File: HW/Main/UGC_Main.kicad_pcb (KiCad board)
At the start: 4 copper layers, 125.7 x 76.4 mm, 135 parts, among them J1 Rumble, J10 Conn_01x01_Pin, J11 Conn_01x01_Pin, J12 Conn_01x01_Pin, J13 503480-0640, J14 USB4105-GF-A-060, J2 LT, J3 RT, J4 Conn_01x06_Pin, J5 Conn_01x01_Pin, J6 Conn_01x01_Pin, J7 Conn_01x01_Pin, J8 Conn_01x01_Pin, J9 Conn_01x01_Pin, Q1 MMBT3904, Q2 MMBT3904, Q3 BSS138DW, Q4 BSS138DW, Q5 Q_NMOS_GSD, Q6 Q_PMOS_GDS, Q7 Q_NMOS_GSD, SW1 SW_Push, SW10 SW_Push, SW11 SW_Push, SW12 SW_Push, SW13 SW_Push, SW14 TS09-63-25-R-260-SMT, SW2 SW_Push, SW3 SW_Push, SW4 SW_Push, SW5 SW_Push, SW6 GL18_SW, SW7 SW_Push, SW8 SW_Push, SW9 TS09-63-25-R-260-SMT, U1 ESP32-PICO-MINI-02, U10 ST_LSM6, U11 BQ25180, U12 CH340K, U13 PI3USB4000A, U2 GH39F (Hall SOT23), U3 GH39F (Hall SOT23), U4 TPS630001RCR, U5 ST_LSM6, U6 MCP3002, U7 MCP3002, U8 RP2040, U9 GD25Q80EEIGR, Y1 Crystal_GND3

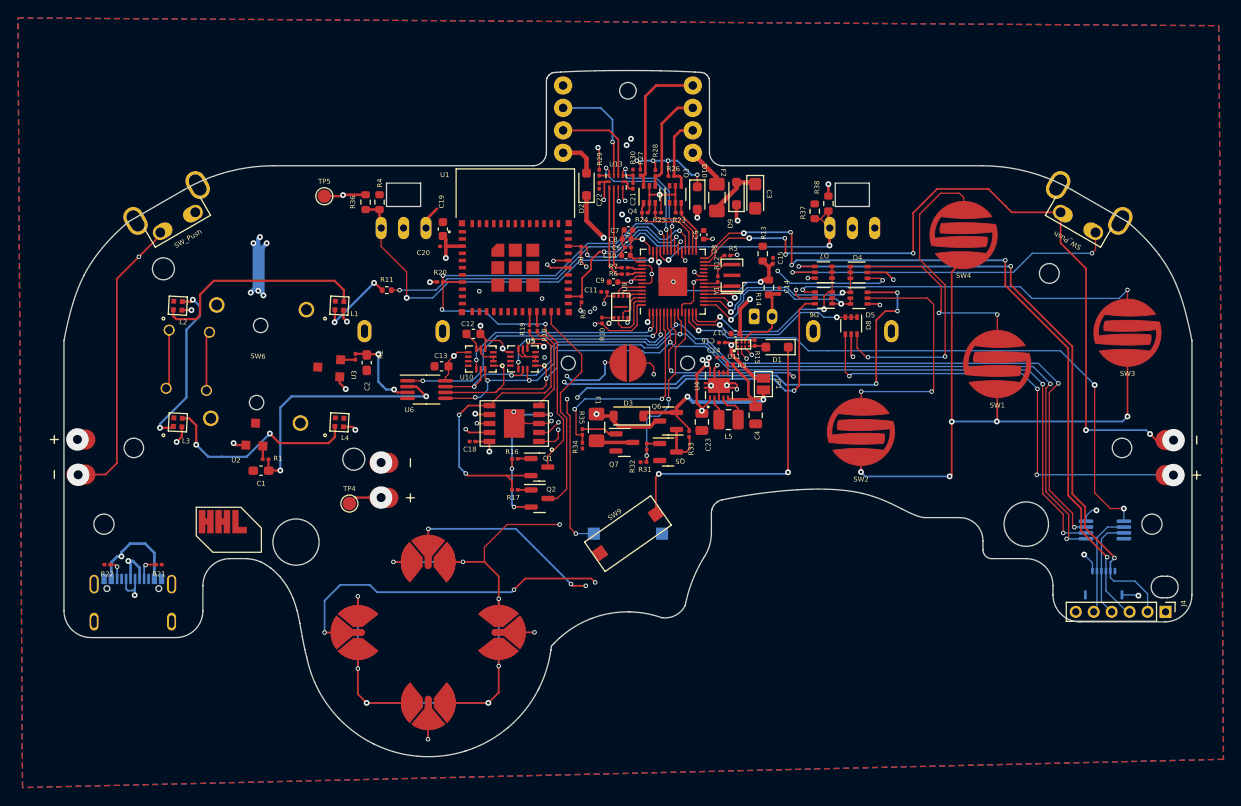
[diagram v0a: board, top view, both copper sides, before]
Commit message: Unify USB C connector
Unified USB-C Connection
Reliability issues present with type C pogo pin board
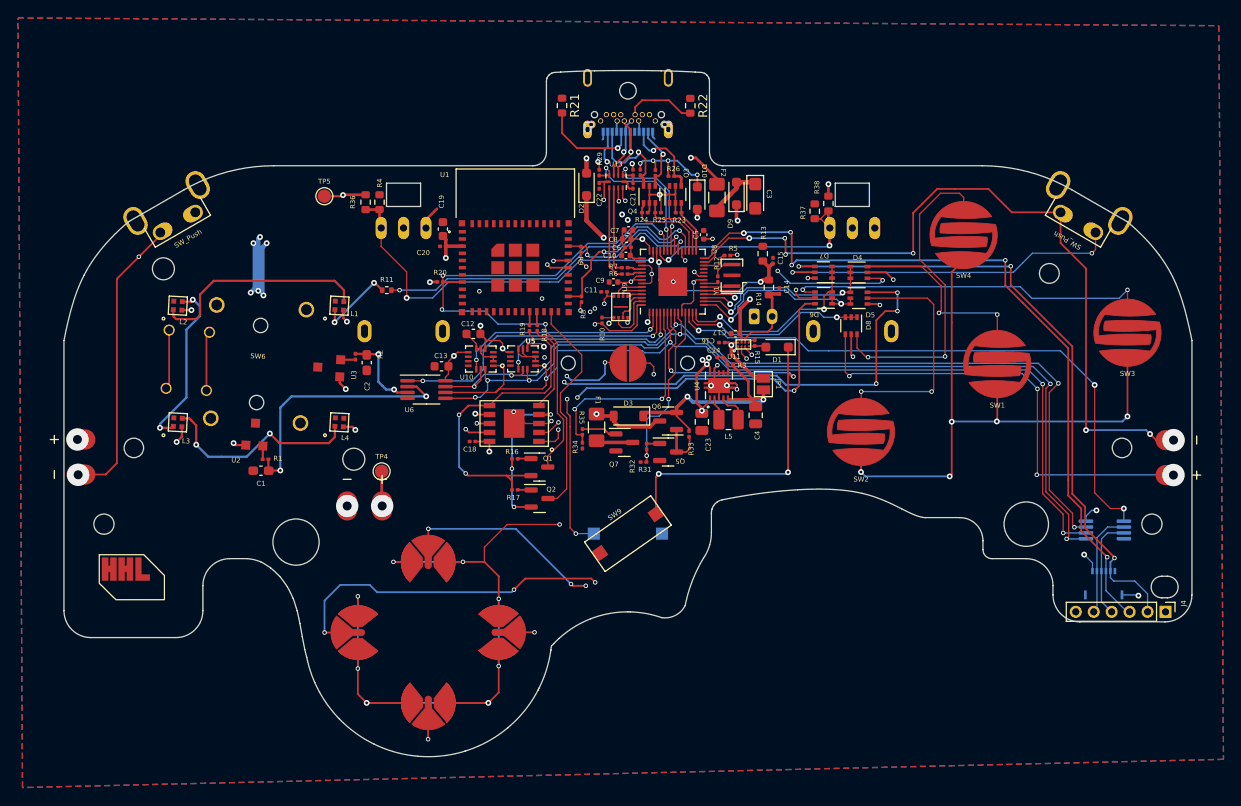
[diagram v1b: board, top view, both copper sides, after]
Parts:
- removed J10, J11, J12, J6, J7, J8, J9: Conn_01x01_Pin, hhl:YZ72015053P-01
- removed J14: USB4105-GF-A-060, hhl:GCT_USB4105-GF-A-060
- J5: value Conn_01x01_Pin -> UJ31-CH-G1-SMT-TR; footprint hhl:YZ72015053P-01 -> hhl:CUI_UJ31-CH-G1-SMT-TR
- R21, R22: value 5.1k -> 5.1kohm; footprint Resistor_SMD:R_0201_0603Metric -> Resistor_SMD:R_0603_1608Metric
- moved R22 82.7 mm to (225.4, 87.8), turned to -90 degrees
- moved R21 68.1 mm to (211.1, 87.8), turned to -90 degrees
- moved REF** 12.0 mm to (162.5, 140.8)
- moved J5 6.83 mm to (215.7, 90.7), turned to 0 degrees
- moved TP4 5.07 mm to (191.0, 128.6)
- moved J1 1.96 mm to (190.3, 132.4), turned to -90 degrees
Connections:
- R21 pad 2: Net-(J14-CC1) -> CC1
- R22 pad 1: Net-(J14-CC2) -> GND
- R22 pad 2: GND -> CC2
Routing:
- net D+: track 120.5 -> 6.93 mm, vias 2 -> 1
- net D-: track 113.1 -> 9.27 mm
- net +5V_PRE: track 110.0 -> 14.8 mm
- net +3V3_PRE: track 4.62 -> 23.1 mm, vias 0 -> 2
- net CC1: track 0.00 -> 11.1 mm, vias 0 -> 1
- net N_LATCH: track 8.51 -> 16.7 mm, vias 0 -> 1
- net CC2: track 0.00 -> 7.89 mm
- net RUMBLE-: track 35.5 -> 42.5 mm
- net N_DATA: track 11.6 -> 16.2 mm, vias 0 -> 1
- net Net-(J14-CC1): track 2.79 -> 0.00 mm, vias 1 -> 0
- net Net-(J14-CC2): track 2.23 -> 0.00 mm, vias 1 -> 0
- net VBUS_SYS: track 102.2 -> 103.4 mm
- net GND: track 40.4 -> 41.3 mm, vias 19 -> 18
- net SHARED_PU: track 12.8 -> 12.1 mm
- net N_CLOCK: track 16.2 -> 16.0 mm, vias 0 -> 1

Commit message: PCB Update
- Add RESET switch
- Add ESP bootloader switch
- Adjust screw holes for trigger bracket mount
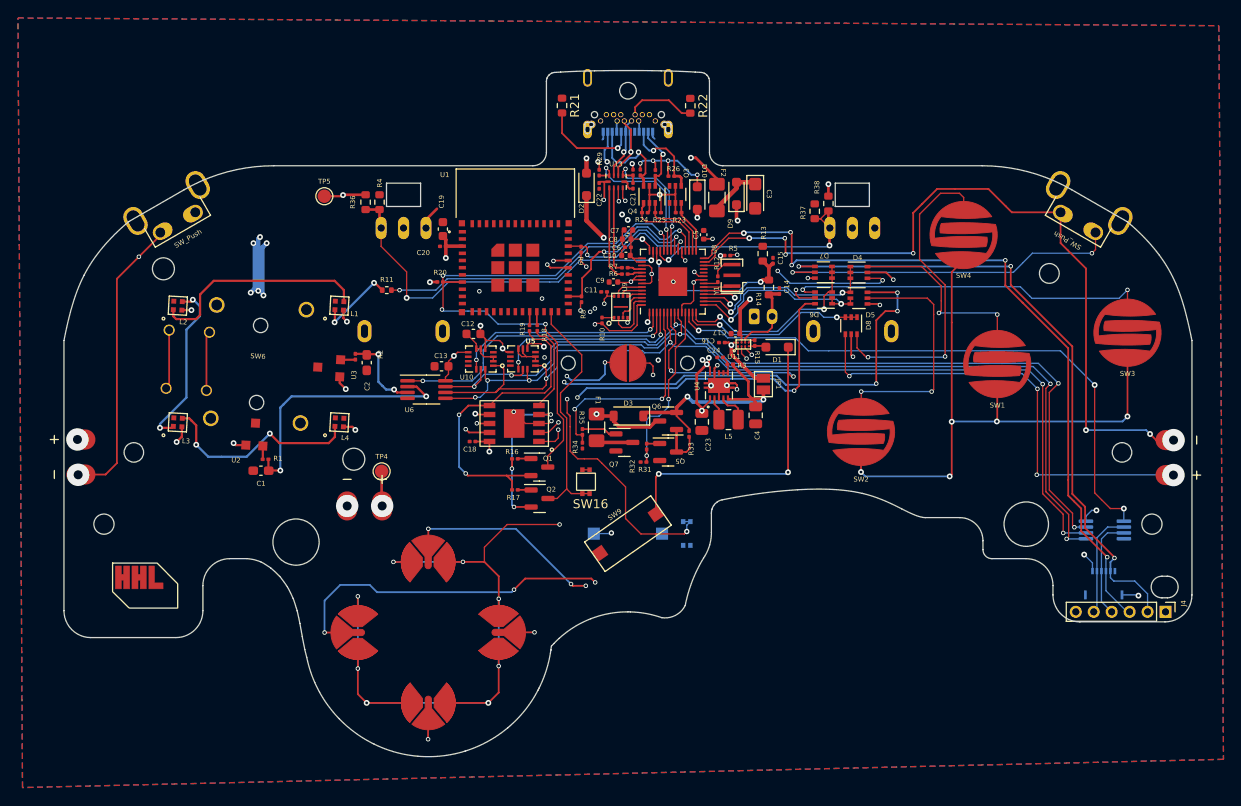
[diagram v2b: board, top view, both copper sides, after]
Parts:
- added SW15: 1TS026A-1000-0550, hhl:1TS026A-1000-0550, B.Cu at (225.0, 135.5)
- added SW16: 1TS026A-1000-0550, hhl:1TS026A-1000-0550, F.Cu at (213.8, 129.7)
- moved REF** 1.75 mm to (164.0, 141.7)
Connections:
- R5 pad 2: /RUN -> RP_RUN
- SW14 pad 2: USB_BOOT -> RP_RUN
- U8 pad 26: /RUN -> RP_RUN
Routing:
- net RP_RUN: track 0.00 -> 53.2 mm, vias 0 -> 3
- net USB_BOOT: track 35.4 -> 45.1 mm
- net /RUN: track 3.13 -> 0.00 mm
- net ESP_IO0: track 24.9 -> 27.7 mm
- net GND: track 41.3 -> 42.1 mm
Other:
- outline, holes or cut-outs redrawn
- board text added: "GC Ultimate r1 Designed By Mitch"
- board text added: "MOTOR"
